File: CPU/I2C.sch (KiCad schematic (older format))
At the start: 37 parts, among them J302 1X4SMD-FPC, J303 Conn_02x03_Odd_Even, Q301 IRLML0040TR, U201 OPT3001, U202 ATTINY84ATTINY84-20PU

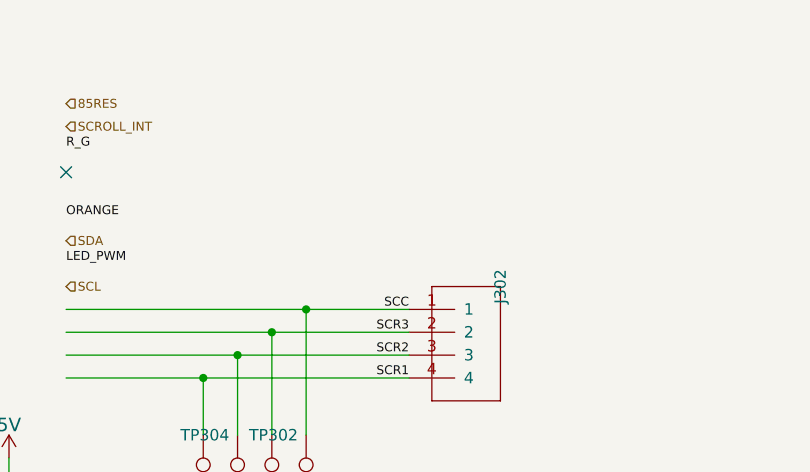
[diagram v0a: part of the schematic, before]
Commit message: Corrected the issues with v1 of the CPU board. Moved to 0.8mm board. Should be ready for another order.
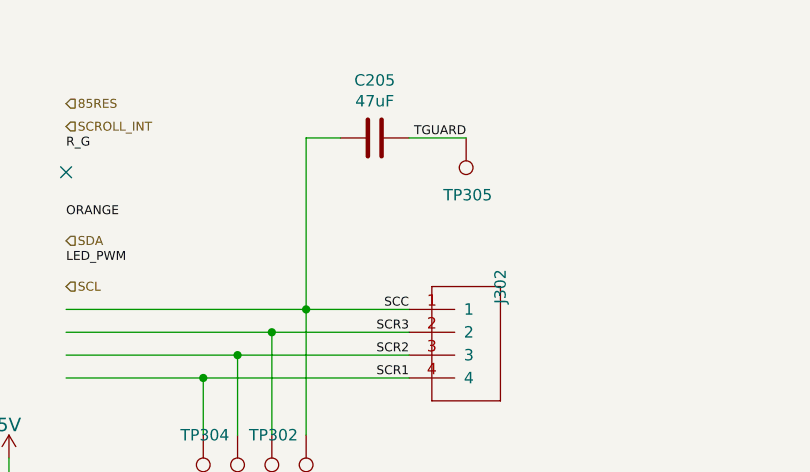
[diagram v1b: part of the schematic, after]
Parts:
- added C205: 47uF, Capacitor_SMD:C_0805_2012Metric_Pad1.15x1.40mm_HandSolder, symbol Device:C
- added TP305: TestPoint, TestPoint:TestPoint_Pad_D1.0mm, symbol Connector:TestPoint
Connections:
- net labels added: TGUARD
- wire segments 85 -> 88
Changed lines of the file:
@@
 Connection ~ 8550 2150
 NoConn ~ 7500 1550
+$Comp
+L Connector:TestPoint TP?
+U 1 1 5EADA810
+P 9250 1400
+AR Path="/5EADA810" Ref="TP?"  Part="1"
+AR Path="/5E916134/5EADA810" Ref="TP305"  Part="1"
+AR Path="/5E9D5ED5/5EADA810" Ref="TP?"  Part="1"
+F 0 "TP305" H 9350 1650 50  0000 R CNN
+F 1 "TestPoint" H 9192 1517 50  0001 R CNN
+F 2 "TestPoint:TestPoint_Pad_D1.0mm" H 9450 1400 50  0001 C CNN
+F 3 "~" H 9450 1400 50  0001 C CNN
+	1    9250 1400
+	-1   0    0    1
+$EndComp
+Text Label 9250 1400 2    39   ~ 0
+TGUARD
+$Comp
+L Device:C C?
+U 1 1 5EADA819
+P 8850 1400
+AR Path="/5EADA819" Ref="C?"  Part="1"
+AR Path="/5E916134/5EADA819" Ref="C205"  Part="1"
+F 0 "C205" V 9102 1400 50  0000 C CNN
+F 1 "47uF" V 9011 1400 50  0000 C CNN
+F 2 "Capacitor_SMD:C_0805_2012Metric_Pad1.15x1.40mm_HandSolder" H 8888 1250 50  0001 C CNN
+F 3 "~" H 8850 1400 50  0001 C CNN
+F 4 " C28323" H 8850 1400 50  0001 C CNN "LCSC Part Number"
+F 5 "C0805C105K3RACTU" H 8850 1400 50  0001 C CNN "DigiKey"
+	1    8850 1400
+	0    -1   -1   0
+$EndComp
+Wire Wire Line
+	8550 1400 8700 1400
+Wire Wire Line
+	9000 1400 9250 1400
+Wire Wire Line
+	8550 1400 8550 2150
 $EndSCHEMATC

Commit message: Rewiring the T84 to the 5 volt line.
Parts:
- added RX301, TX301: TestPoint, TestPoint:TestPoint_Pad_D1.0mm, symbol Connector:TestPoint
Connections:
- net labels added: GREEN, RED, SCL5, SDA5
- net labels removed: R_G
- wire segments 88 -> 94
- no-connect marks 1 -> 0
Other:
- moved on the sheet: D310B, R310

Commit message: Moving signals to accomodate charger sensing.
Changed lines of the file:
@@
 $EndComp
-Wire Wire Line
-	7550 1450 8150 1450
 Wire Wire Line
 	8150 1450 8150 1600
@@
 Text HLabel 7250 3150 2    39   Input ~ 0
 SDA5
+Wire Wire Line
+	7500 1450 8150 1450
 $EndSCHEMATC

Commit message: Updates from CPU v1 were completed. Switched out Tiny84 for a tiny1614 because the 84 lacks a hardware twi driver. This version was sent to production at jlcpcb.
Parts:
- removed U202: ATTINY84ATTINY84-20PU, MarcoK:14SOIC, symbol UltraLibrarian:ATTINY84ATTINY84-20PU
- added U202: ATtiny1614-SS, Package_SO:SOIC-14_3.9x8.7mm_P1.27mm, symbol MarcoK:ATtiny1604-SS
- R301, R302, R303, R304, R305, R306, R307, R308, R309: footprint CPU:R1206 -> Resistor_SMD:R_0805_2012Metric_Pad1.15x1.40mm_HandSolder; DigiKey RC1206FR-07330RL -> RC0805FR-07330RL; LCSC Part Number C17930 -> C17630
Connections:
- net labels added: UPDI
- wire segments 94 -> 97
- no-connect marks 0 -> 3
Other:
- moved on the sheet: C205, J302, J303, RX301, TP301, TP302, TP303, TP304, TP305, TX301

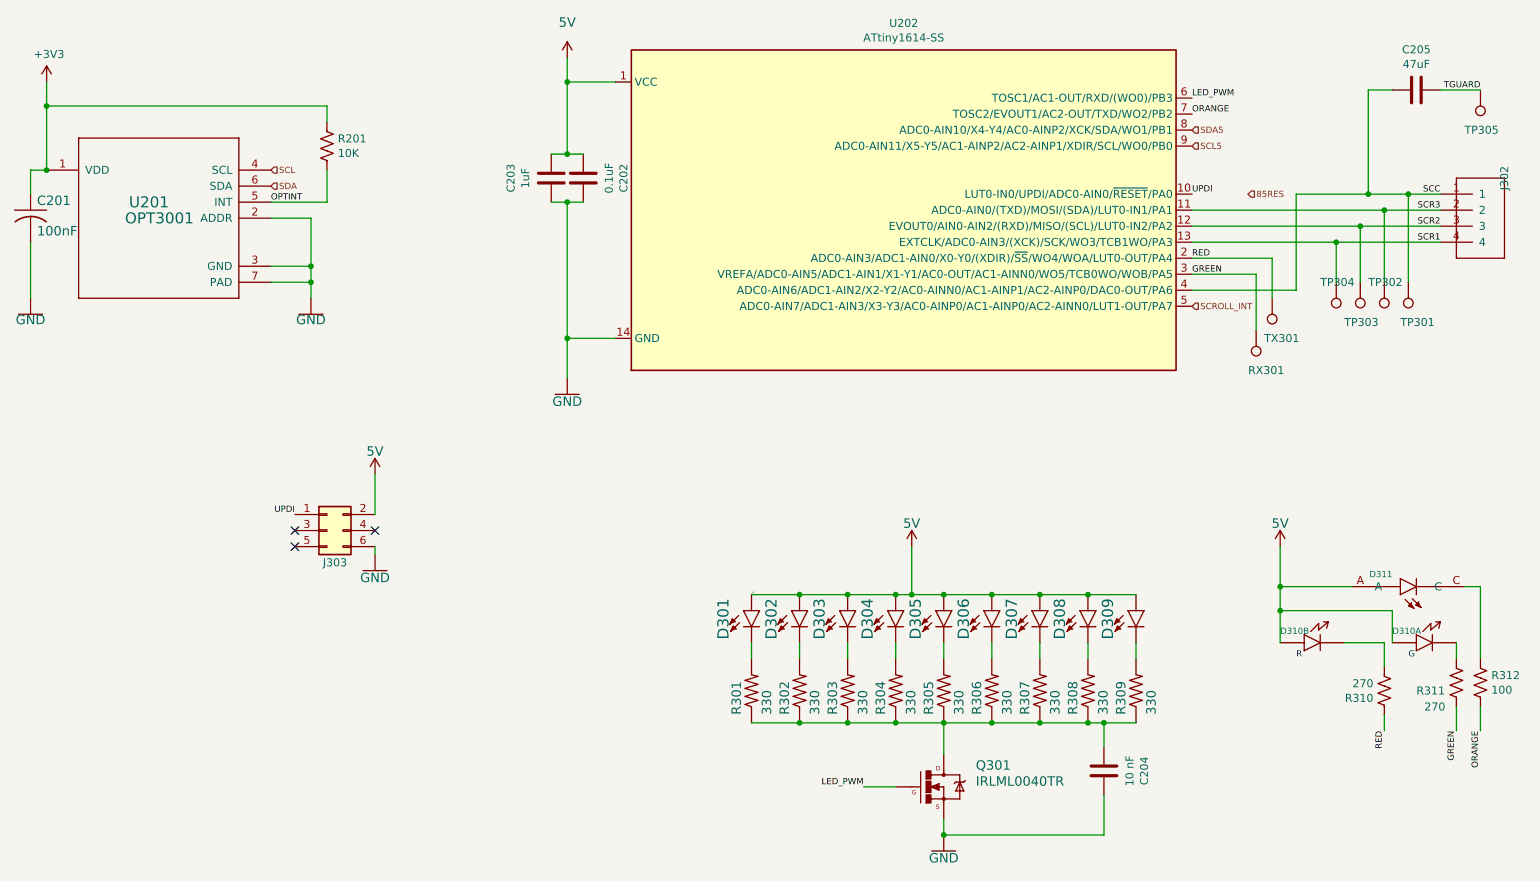
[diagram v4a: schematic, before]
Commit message: Add display circuitry.
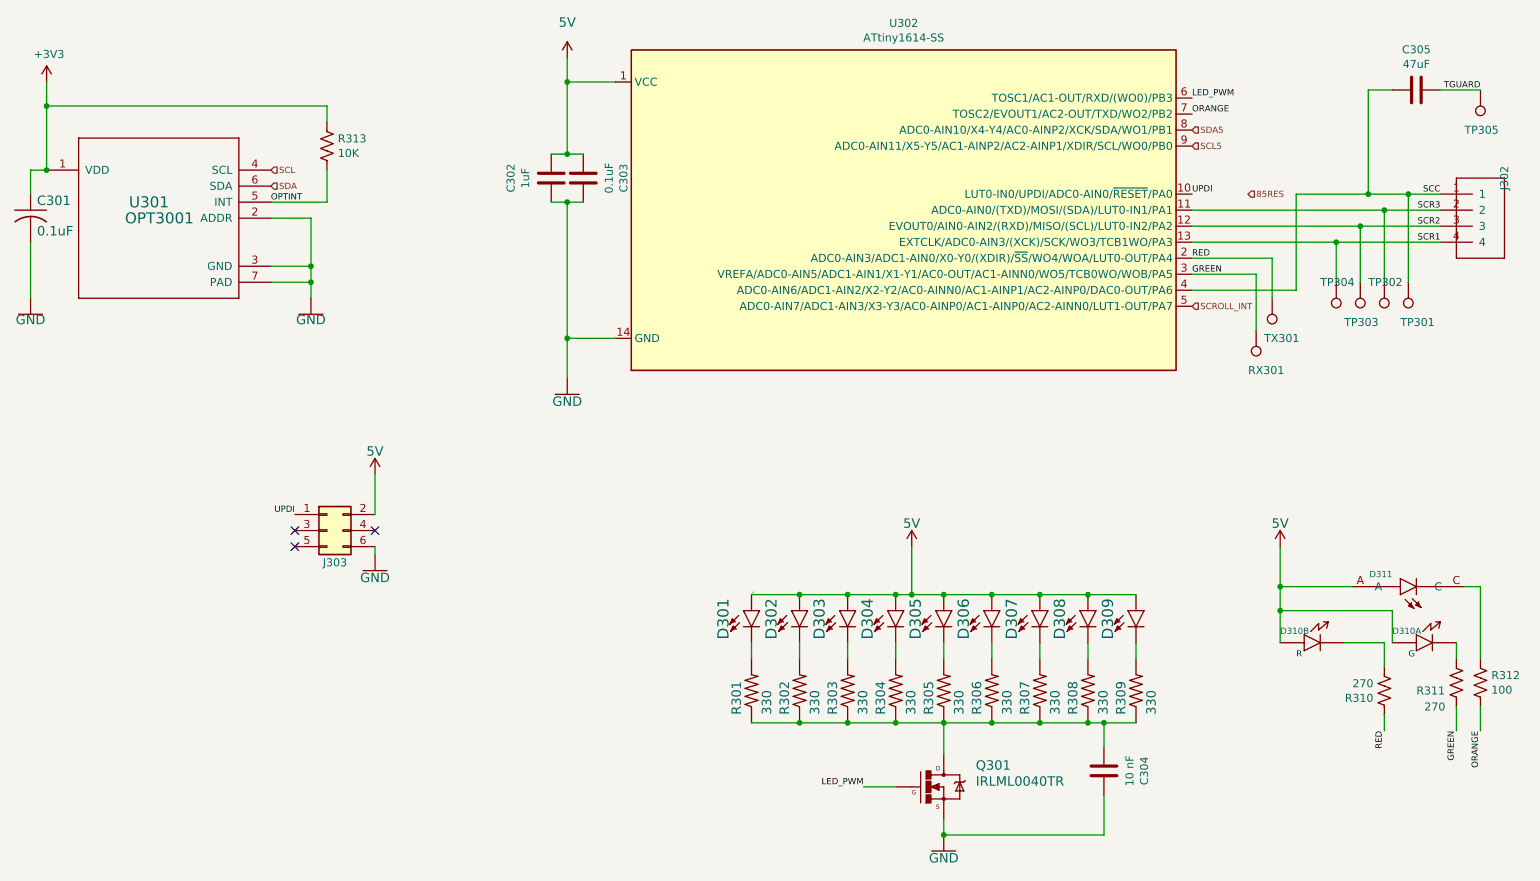
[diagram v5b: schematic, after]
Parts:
- C301: renamed from C201; value 100nF -> 0.1uF; Customer Reference (none) -> CR101-V3; DigiKey CC0805KRX7R8BB104 -> C0805C104K3RACTU
- C302: renamed from C203; Customer Reference (none) -> CR101-V3
- C303: renamed from C202; Customer Reference (none) -> CR101-V3; DigiKey CL21B104KACNNNC -> C0805C104K3RACTU
- C304: renamed from C204; Customer Reference (none) -> CR101-V3; DigiKey C0805C103K3RACTU -> GRM216R71C103MA01D; LCSC Part Number C1710 -> C15850
- C305: renamed from C205; Customer Reference (none) -> CR101-V3; DigiKey C0805C105K3RACTU -> 1276-6800-1-ND
- D301, D302, D303, D304, D305, D306, D307, D308, D309, D310, D311, J302, Q301, R301, R302, R303, R304, R305, R306, R307, R308, R309, R312, TP303, TP304: Customer Reference (none) -> CR101-V3
- J303: Customer Reference (none) -> CR101-V3; DigiKey 818-22-006-10-002101, 818-22-006-10-005101 -> 818-22-006-10-002101
- R310, R311: Customer Reference (none) -> CR101-V3; DigiKey RMCF0805FT270R -> RC0805FR-07330RL
- R313: renamed from R201; Customer Reference (none) -> CR101-V3
- RX301, TP301, TX301: Customer Reference (none) -> CR101-V3; DigiKey ‎709150001040006 -> (none)
- TP302: Customer Reference (none) -> CR101-V3; DigiKey 709150001030006 -> (none)
- TP305: Customer Reference (none) -> CR101-V3; DigiKey (none) -> 709150001030006
- U301: renamed from U201; Customer Reference (none) -> CR101-V3
- U302: renamed from U202; Customer Reference (none) -> CR101-V3; DigiKey (none) -> ATTINY1614-SSNRCT-ND

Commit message: Move to separate branch to track CPU development separately.
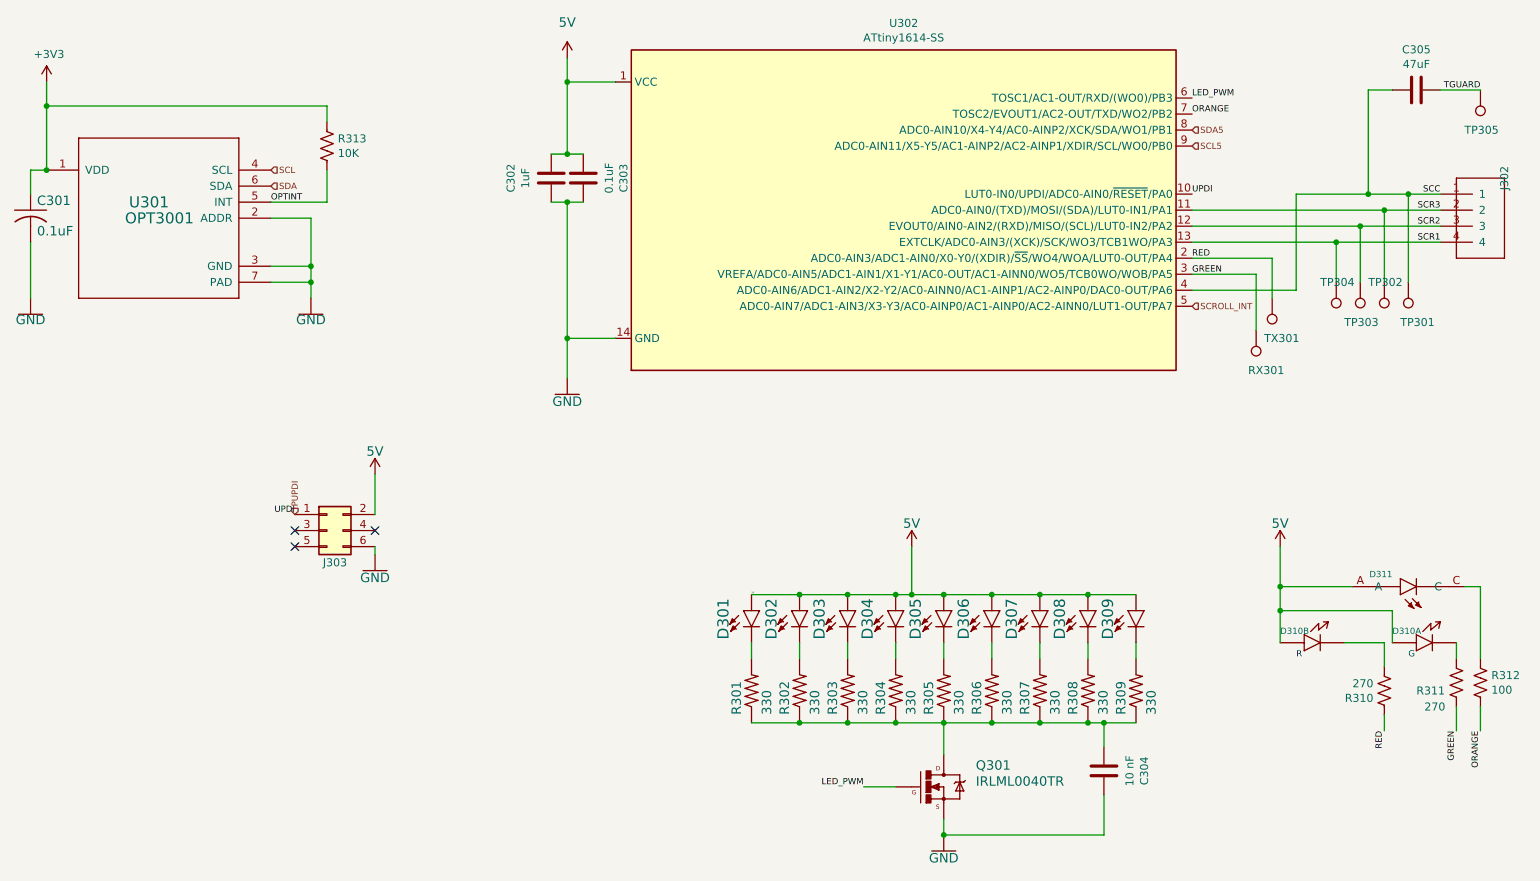
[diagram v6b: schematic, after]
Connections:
- net UPDI renamed PUPDI
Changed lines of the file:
@@
 $EndComp
 $Comp
-L CPU-eagle-import:5V #SUPPLY0102
+L CPU-eagle-import:5V #SUPPLY0106
 U 1 1 5EB5869E
 P 5200 1100
-F 0 "#SUPPLY0102" H 5200 1100 50  0001 C CNN
+F 0 "#SUPPLY0106" H 5200 1100 50  0001 C CNN
 F 1 "5V" H 5200 1322 59  0000 C CNN
 F 2 "" H 5200 1100 50  0001 C CNN
@@
 	1    0    0    -1
 $EndComp
-Text HLabel 9450 1950 2    39   Input ~ 0
-85RES
 Wire Wire Line
 	5200 2000 5200 2850
@@
 Text Label 3500 3950 2    39   ~ 0
 UPDI
+Text HLabel 3500 3950 1    39   Input ~ 0
+PUPDI
 $EndSCHEMATC

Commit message: Version 4 of the CPU board ordered with this commit.
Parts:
- C301, C303: LCSC Part Number C49678 -> C49678
- C304: LCSC Part Number C15850 -> C1710
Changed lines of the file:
@@
 F 2 "Capacitor_SMD:C_0805_2012Metric_Pad1.15x1.40mm_HandSolder" H 1850 2050 50  0001 C CNN
 F 3 "" H 1850 2050 50  0001 C CNN
-F 4 " C49678" H 1850 2050 50  0001 C CNN "LCSC Part Number"
+F 4 "C49678" H 1850 2050 50  0001 C CNN "LCSC Part Number"
 F 5 "C0805C104K3RACTU" H 1850 2050 50  0001 C CNN "DigiKey"
 F 6 "CR101-V3" H 1850 2050 50  0001 C CNN "Customer Reference"
@@
 F 2 "Capacitor_SMD:C_0805_2012Metric_Pad1.15x1.40mm_HandSolder" H 5338 1700 50  0001 C CNN
 F 3 "~" H 5300 1850 50  0001 C CNN
-F 4 " C49678" H 5300 1850 50  0001 C CNN "LCSC Part Number"
+F 4 "C49678" H 5300 1850 50  0001 C CNN "LCSC Part Number"
 F 5 "C0805C104K3RACTU" H 5300 1850 50  0001 C CNN "DigiKey"
 F 6 "CR101-V3" H 5300 1850 50  0001 C CNN "Customer Reference"
@@
 F 2 "Capacitor_SMD:C_0805_2012Metric_Pad1.15x1.40mm_HandSolder" H 8588 5400 50  0001 C CNN
 F 3 "~" H 8550 5550 50  0001 C CNN
-F 4 " C15850" H 8550 5550 50  0001 C CNN "LCSC Part Number"
+F 4 "C1710" H 8550 5550 50  0001 C CNN "LCSC Part Number"
 F 5 "GRM216R71C103MA01D" H 8550 5550 50  0001 C CNN "DigiKey"
 F 6 "CR101-V3" H 8550 5550 50  0001 C CNN "Customer Reference"
